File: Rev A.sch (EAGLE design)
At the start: 21 parts

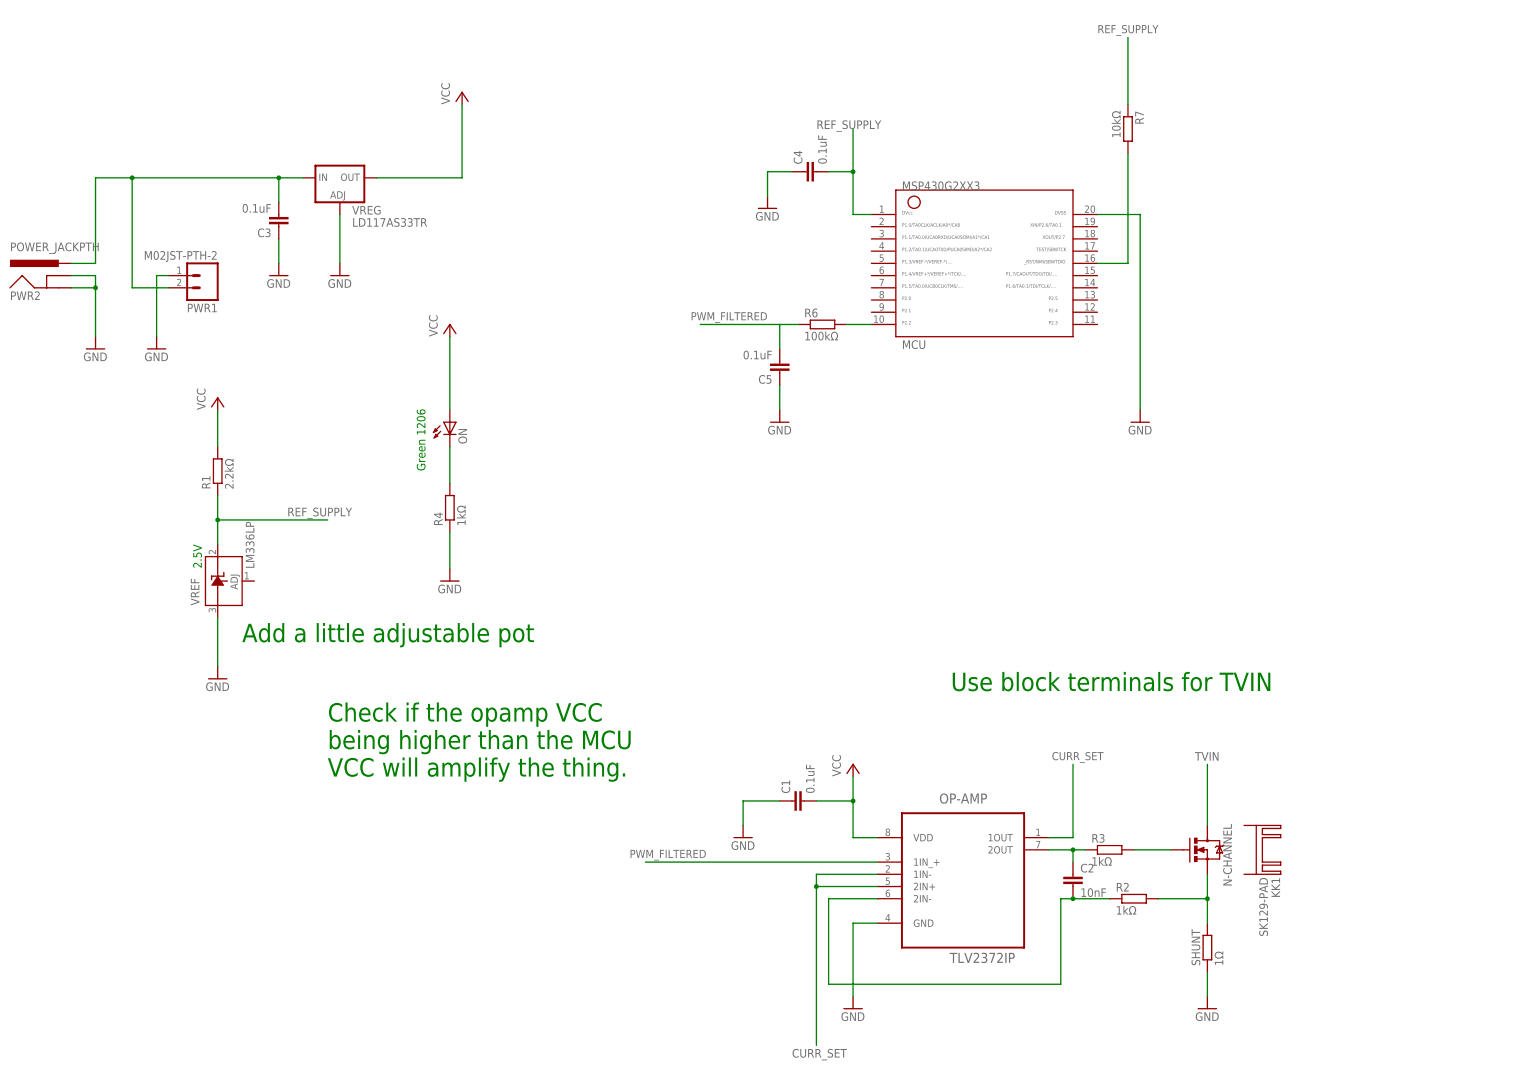
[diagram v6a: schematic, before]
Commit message: Started working on some blocks on the PCB design
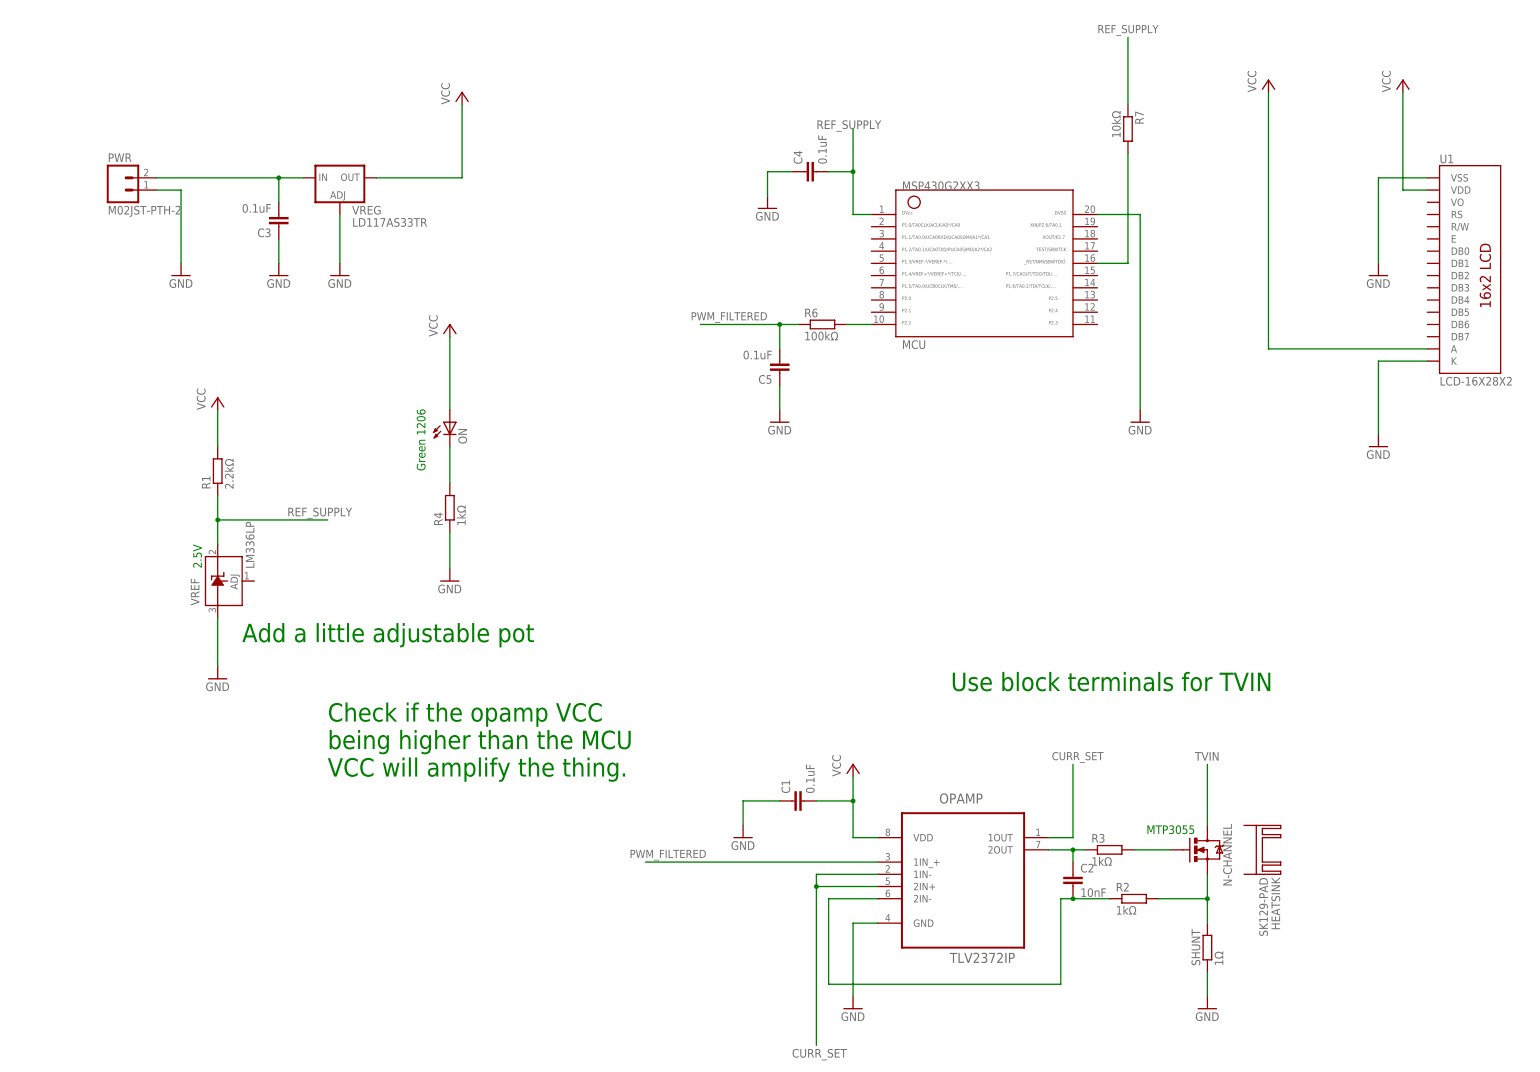
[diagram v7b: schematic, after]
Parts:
- removed PWR1: M02JST-PTH-2, SparkFun-Connectors:M02JST-PTH-2
- removed PWR2: POWER_JACKPTH, SparkFun-Connectors:POWER_JACKPTH
- added PWR: M02JST-PTH-2, SparkFun-Connectors:M02JST-PTH-2
- added U1: LCD-16X28X2, SparkFun-Displays:LCD-16X28X2
- renumbered KK1 to HEATSINK, OP-AMP to OPAMP
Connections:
- net GND: now also PWR.1, U1.K, U1.VSS; no longer PWR1.1, PWR2.GND, PWR2.GNDBREAK
- net N$6: now also PWR.2; no longer PWR1.2, PWR2.PWR
- net VCC: now also U1.A, U1.VDD
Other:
- note added: "MTP3055"
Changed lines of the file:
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@@
 </classes>
 <parts>
-<part name="OP-AMP" library="Texas Instruments_By_element14_Batch_1" deviceset="TLV2372IP" device=""/>
+<part name="OPAMP" library="Texas Instruments_By_element14_Batch_1" deviceset="TLV2372IP" device=""/>
 <part name="P+1" library="supply1" deviceset="VCC" device=""/>
 <part name="GND1" library="supply1" deviceset="GND" device=""/>
@@
 <part name="R3" library="rcl" deviceset="R-EU_" device="R0805" value="1kΩ"/>
 <part name="C2" library="rcl" deviceset="C-EU" device="C0805" value="10nF"/>
-<part name="KK1" library="heatsink" deviceset="SK129-PAD" device=""/>
-<part name="PWR2" library="SparkFun-Connectors" deviceset="POWER_JACK" device="PTH"/>
-<part name="GND6" library="supply1" deviceset="GND" device=""/>
-<part name="PWR1" library="SparkFun-Connectors" deviceset="M02" device="JST-PTH-2"/>
+<part name="HEATSINK" library="heatsink" deviceset="SK129-PAD" device=""/>
+<part name="PWR" library="SparkFun-Connectors" deviceset="M02" device="JST-PTH-2"/>
 <part name="GND4" library="supply1" deviceset="GND" device=""/>
 <part name="VREG" library="v-reg" deviceset="LD117A?*" device="S" technology="33TR"/>
@@
 <part name="GND13" library="supply1" deviceset="GND" device=""/>
 <part name="R7" library="resistor" deviceset="R-EU_" device="R0805" value="10kΩ"/>
+<part name="U1" library="SparkFun-Displays" deviceset="LCD-16X2" device="8X2"/>
+<part name="P+5" library="supply1" deviceset="VCC" device=""/>
+<part name="GND6" library="supply1" deviceset="GND" device=""/>
+<part name="P+6" library="supply1" deviceset="VCC" device=""/>
+<part name="GND12" library="supply1" deviceset="GND" device=""/>
 </parts>
 <sheets>
@@
 being higher than the MCU
 VCC will amplify the thing.</text>
+<text x="200.66" y="38.1" size="1.778" layer="91" rot="R180">MTP3055</text>
 </plain>
 <instances>
-<instance part="OP-AMP" gate="A" x="152.4" y="30.48"/>
+<instance part="OPAMP" gate="A" x="152.4" y="30.48"/>
 <instance part="P+1" gate="VCC" x="129.54" y="50.8"/>
 <instance part="GND1" gate="1" x="129.54" y="0"/>
@@
 <instance part="R3" gate="G$1" x="182.88" y="33.02"/>
 <instance part="C2" gate="G$1" x="175.26" y="27.94"/>
-<instance part="KK1" gate="G$1" x="213.36" y="33.02" rot="R270"/>
-<instance part="PWR2" gate="G$1" x="-35.56" y="147.32"/>
-<instance part="GND6" gate="1" x="-27.94" y="137.16"/>
-<instance part="PWR1" gate="G$1" x="-5.08" y="152.4" rot="R180"/>
-<instance part="GND4" gate="1" x="-15.24" y="137.16"/>
+<instance part="HEATSINK" gate="G$1" x="213.36" y="33.02" rot="R270"/>
+<instance part="PWR" gate="G$1" x="-22.86" y="170.18"/>
+<instance part="GND4" gate="1" x="-10.16" y="152.4"/>
 <instance part="VREG" gate="G$1" x="22.86" y="172.72"/>
 <instance part="GND5" gate="1" x="22.86" y="152.4"/>
@@
 <instance part="GND13" gate="1" x="114.3" y="121.92"/>
 <instance part="R7" gate="G$1" x="186.69" y="182.88" rot="R270"/>
+<instance part="U1" gate="G$1" x="259.08" y="152.4"/>
+<instance part="P+5" gate="VCC" x="243.84" y="193.04"/>
+<instance part="GND6" gate="1" x="238.76" y="152.4"/>
+<instance part="P+6" gate="VCC" x="215.9" y="193.04"/>
+<instance part="GND12" gate="1" x="238.76" y="116.84"/>
 </instances>
 <busses>
@@
 <net name="GND" class="0">
 <segment>
-<pinref part="OP-AMP" gate="A" pin="GND"/>
+<pinref part="OPAMP" gate="A" pin="GND"/>
 <pinref part="GND1" gate="1" pin="GND"/>
 <wire x1="134.62" y1="17.78" x2="129.54" y2="17.78" width="0.1524" layer="91"/>
@@
 </segment>
 <segment>
-<pinref part="PWR2" gate="G$1" pin="GNDBREAK"/>
-<wire x1="-33.02" y1="152.4" x2="-27.94" y2="152.4" width="0.1524" layer="91"/>
-<wire x1="-27.94" y1="152.4" x2="-27.94" y2="149.86" width="0.1524" layer="91"/>
-<junction x="-27.94" y="149.86"/>
-<wire x1="-27.94" y1="149.86" x2="-27.94" y2="139.7" width="0.1524" layer="91"/>
-<pinref part="PWR2" gate="G$1" pin="GND"/>
-<wire x1="-33.02" y1="149.86" x2="-27.94" y2="149.86" width="0.1524" layer="91"/>
-<pinref part="GND6" gate="1" pin="GND"/>
-</segment>
-<segment>
-<pinref part="PWR1" gate="G$1" pin="1"/>
-<wire x1="-12.7" y1="152.4" x2="-15.24" y2="152.4" width="0.1524" layer="91"/>
-<wire x1="-15.24" y1="152.4" x2="-15.24" y2="139.7" width="0.1524" layer="91"/>
+<pinref part="PWR" gate="G$1" pin="1"/>
+<wire x1="-15.24" y1="170.18" x2="-10.16" y2="170.18" width="0.1524" layer="91"/>
+<wire x1="-10.16" y1="170.18" x2="-10.16" y2="154.94" width="0.1524" layer="91"/>
 <pinref part="GND4" gate="1" pin="GND"/>
 </segment>
@@
 <pinref part="GND13" gate="1" pin="GND"/>
 </segment>
+<segment>
+<pinref part="GND6" gate="1" pin="GND"/>
+<wire x1="238.76" y1="154.94" x2="238.76" y2="172.72" width="0.1524" layer="91"/>
+<pinref part="U1" gate="G$1" pin="VSS"/>
+<wire x1="238.76" y1="172.72" x2="248.92" y2="172.72" width="0.1524" layer="91"/>
+</segment>
+<segment>
+<pinref part="U1" gate="G$1" pin="K"/>
+<wire x1="248.92" y1="134.62" x2="238.76" y2="134.62" width="0.1524" layer="91"/>
+<wire x1="238.76" y1="134.62" x2="238.76" y2="119.38" width="0.1524" layer="91"/>
+<pinref part="GND12" gate="1" pin="GND"/>
+</segment>
 </net>
 <net name="VCC" class="0">
 <segment>
-<pinref part="OP-AMP" gate="A" pin="VDD"/>
+<pinref part="OPAMP" gate="A" pin="VDD"/>
 <pinref part="P+1" gate="VCC" pin="VCC"/>
 <wire x1="134.62" y1="35.56" x2="129.54" y2="35.56" width="0.1524" layer="91"/>
@@
 <pinref part="P+4" gate="VCC" pin="VCC"/>
 </segment>
+<segment>
+<pinref part="U1" gate="G$1" pin="VDD"/>
+<wire x1="248.92" y1="170.18" x2="243.84" y2="170.18" width="0.1524" layer="91"/>
+<wire x1="243.84" y1="170.18" x2="243.84" y2="190.5" width="0.1524" layer="91"/>
+<pinref part="P+5" gate="VCC" pin="VCC"/>
+</segment>
+<segment>
+<pinref part="U1" gate="G$1" pin="A"/>
+<wire x1="248.92" y1="137.16" x2="215.9" y2="137.16" width="0.1524" layer="91"/>
+<wire x1="215.9" y1="137.16" x2="215.9" y2="190.5" width="0.1524" layer="91"/>
+<pinref part="P+6" gate="VCC" pin="VCC"/>
+</segment>
 </net>
 <net name="N$2" class="0">
@@
 <wire x1="172.72" y1="5.08" x2="124.46" y2="5.08" width="0.1524" layer="91"/>
 <wire x1="124.46" y1="5.08" x2="124.46" y2="22.86" width="0.1524" layer="91"/>
-<pinref part="OP-AMP" gate="A" pin="2IN-"/>
+<pinref part="OPAMP" gate="A" pin="2IN-"/>
 <wire x1="124.46" y1="22.86" x2="134.62" y2="22.86" width="0.1524" layer="91"/>
 <pinref part="R2" gate="G$1" pin="1"/>
@@
 <net name="N$4" class="0">
 <segment>
-<pinref part="OP-AMP" gate="A" pin="2OUT"/>
+<pinref part="OPAMP" gate="A" pin="2OUT"/>
 <pinref part="R3" gate="G$1" pin="1"/>
 <wire x1="170.18" y1="33.02" x2="175.26" y2="33.02" width="0.1524" layer="91"/>
@@
 <net name="CURR_SET" class="0">
 <segment>
-<pinref part="OP-AMP" gate="A" pin="2IN+"/>
+<pinref part="OPAMP" gate="A" pin="2IN+"/>
 <wire x1="134.62" y1="25.4" x2="121.92" y2="25.4" width="0.1524" layer="91"/>
 <wire x1="121.92" y1="25.4" x2="121.92" y2="-7.62" width="0.1524" layer="91"/>
 <label x="116.84" y="-10.16" size="1.778" layer="95"/>
-<pinref part="OP-AMP" gate="A" pin="1IN-"/>
+<pinref part="OPAMP" gate="A" pin="1IN-"/>
 <wire x1="134.62" y1="27.94" x2="121.92" y2="27.94" width="0.1524" layer="91"/>
 <wire x1="121.92" y1="27.94" x2="121.92" y2="25.4" width="0.1524" layer="91"/>
@@
 </segment>
 <segment>
-<pinref part="OP-AMP" gate="A" pin="1OUT"/>
+<pinref part="OPAMP" gate="A" pin="1OUT"/>
 <wire x1="170.18" y1="35.56" x2="175.26" y2="35.56" width="0.1524" layer="91"/>
 <wire x1="175.26" y1="35.56" x2="175.26" y2="50.8" width="0.1524" layer="91"/>
@@
 <net name="N$6" class="0">
 <segment>
-<wire x1="-20.32" y1="172.72" x2="-20.32" y2="149.86" width="0.1524" layer="91"/>
-<pinref part="PWR1" gate="G$1" pin="2"/>
-<wire x1="-20.32" y1="149.86" x2="-12.7" y2="149.86" width="0.1524" layer="91"/>
-<pinref part="PWR2" gate="G$1" pin="PWR"/>
-<wire x1="-33.02" y1="154.94" x2="-27.94" y2="154.94" width="0.1524" layer="91"/>
-<wire x1="-27.94" y1="154.94" x2="-27.94" y2="172.72" width="0.1524" layer="91"/>
 <pinref part="VREG" gate="G$1" pin="IN"/>
-<wire x1="-27.94" y1="172.72" x2="-20.32" y2="172.72" width="0.1524" layer="91"/>
-<junction x="-20.32" y="172.72"/>
-<wire x1="-20.32" y1="172.72" x2="10.16" y2="172.72" width="0.1524" layer="91"/>
+<wire x1="-15.24" y1="172.72" x2="10.16" y2="172.72" width="0.1524" layer="91"/>
 <pinref part="C3" gate="G$1" pin="2"/>
 <wire x1="10.16" y1="172.72" x2="15.24" y2="172.72" width="0.1524" layer="91"/>
 <wire x1="10.16" y1="167.64" x2="10.16" y2="172.72" width="0.1524" layer="91"/>
 <junction x="10.16" y="172.72"/>
+<pinref part="PWR" gate="G$1" pin="2"/>
 </segment>
 </net>
@@
 <wire x1="114.3" y1="142.24" x2="97.79" y2="142.24" width="0.1524" layer="91"/>
 <label x="111.76" y="144.78" size="1.6764" layer="95" rot="R180"/>
-</segment>
-<segment>
-<pinref part="OP-AMP" gate="A" pin="1IN_+"/>
+<junction x="114.3" y="142.24"/>
+</segment>
+<segment>
+<pinref part="OPAMP" gate="A" pin="1IN_+"/>
 <wire x1="134.62" y1="30.48" x2="86.36" y2="30.48" width="0.1524" layer="91"/>
 <label x="99.06" y="33.02" size="1.6764" layer="95" rot="R180"/>

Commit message: Removed the voltage reference
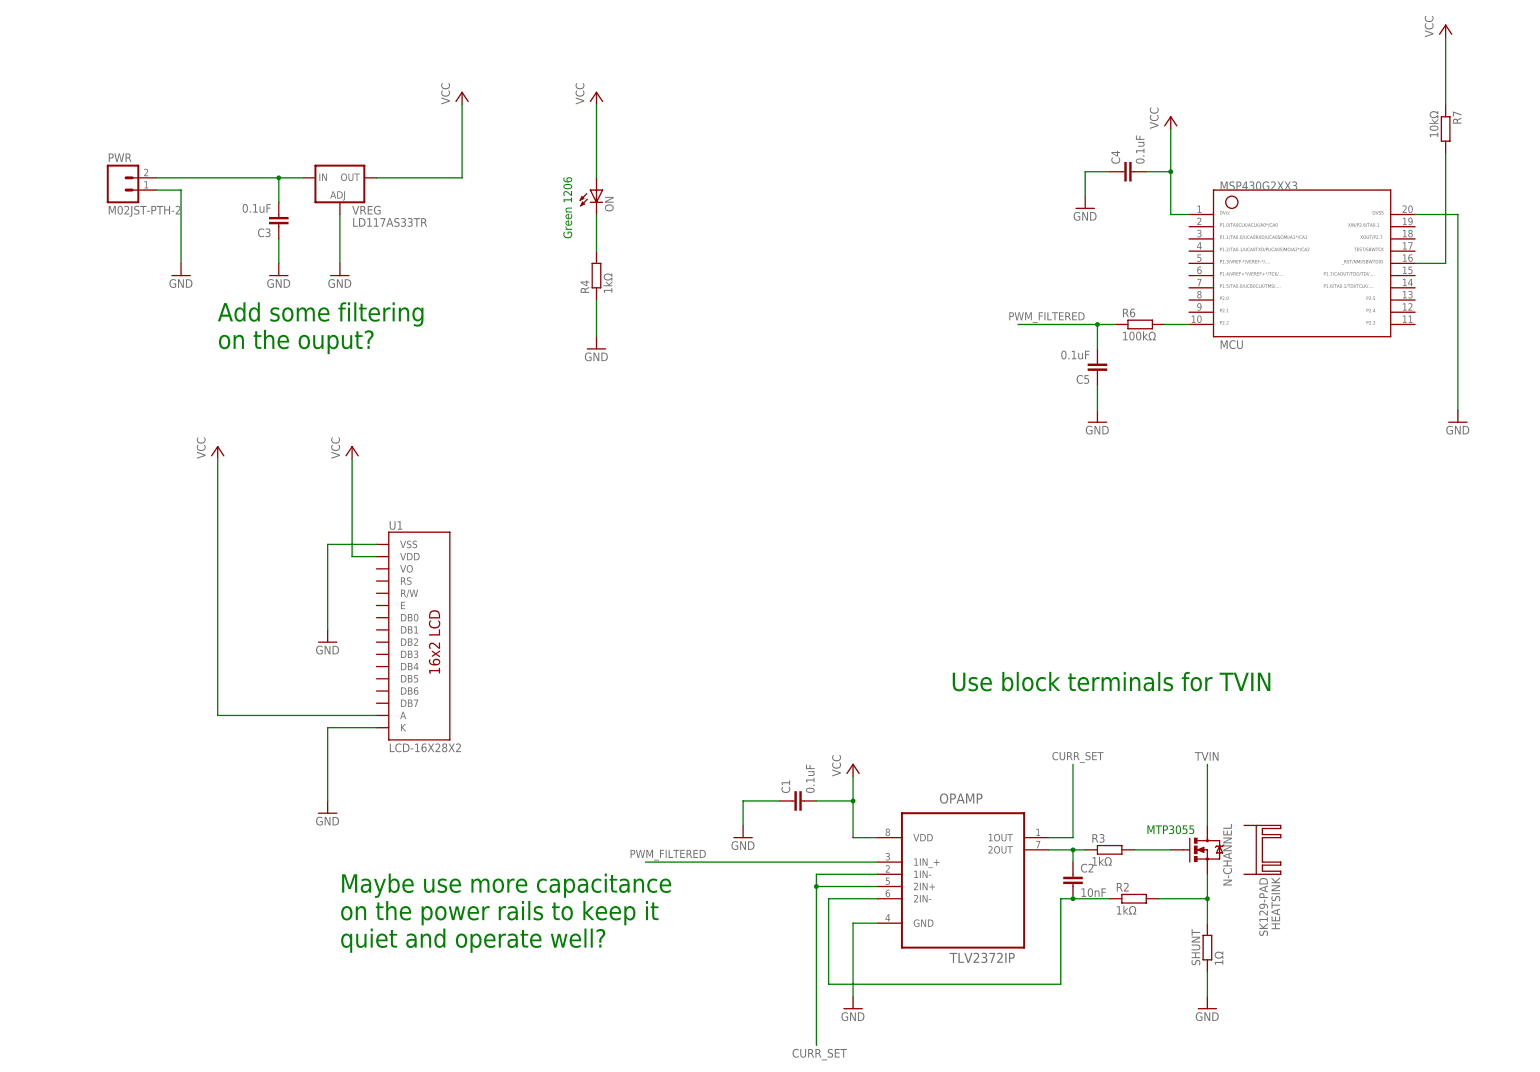
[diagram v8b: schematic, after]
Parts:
- removed R1: 2.2kΩ, rcl:R-EU_R0805
- removed VREF: LM336LP, linear:LM336LP
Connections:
- removed net REF_SUPPLY: C4.2, MCU.1, R1.1, R7.1, VREF.C
- net GND: no longer VREF.A
- net VCC: now also C4.2, MCU.1, R7.1; no longer R1.2
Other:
- note added: "Add some filtering on the ouput?"
- note added: "Maybe use more capacitance on the power rails to keep it quiet and operate well?"
- note removed: "2.5V"
- note removed: "Add a little adjustable pot"
- note removed: "Check if the opamp VCC being higher than the MCU VCC will amplify the thing."
- moved on the sheet: C4, C5, MCU, ON, R4, R6, R7, U1
